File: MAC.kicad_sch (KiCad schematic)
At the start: 5 parts

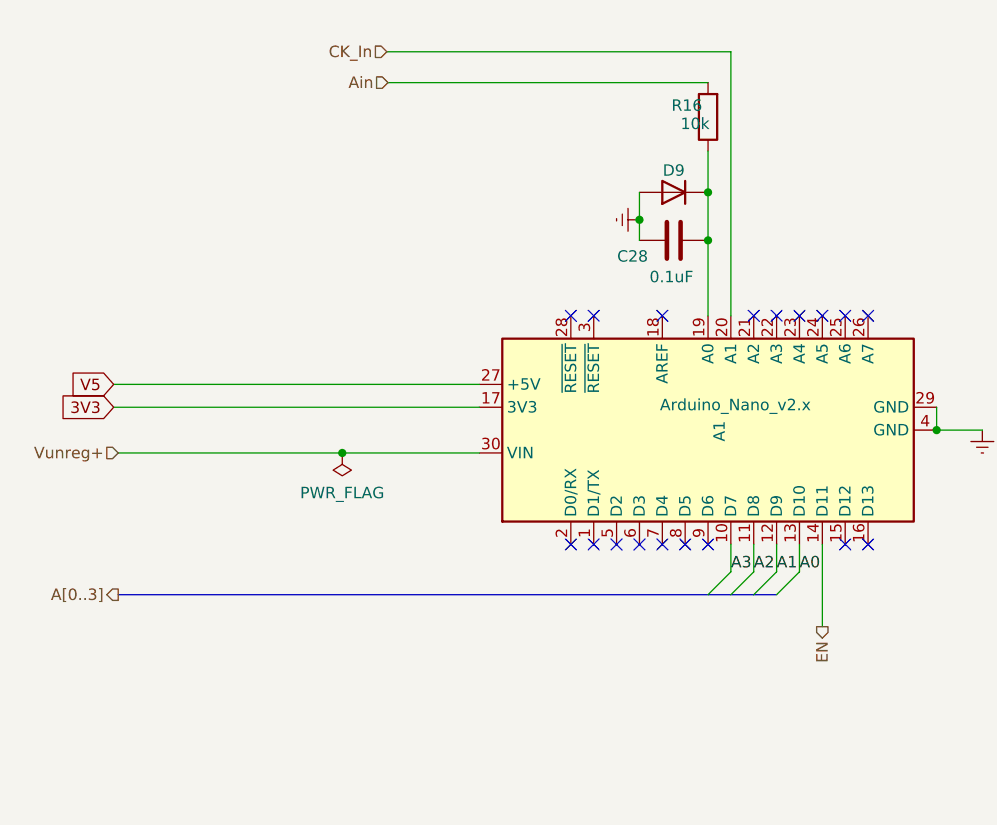
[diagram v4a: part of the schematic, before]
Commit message: Updated improved board for all SMD
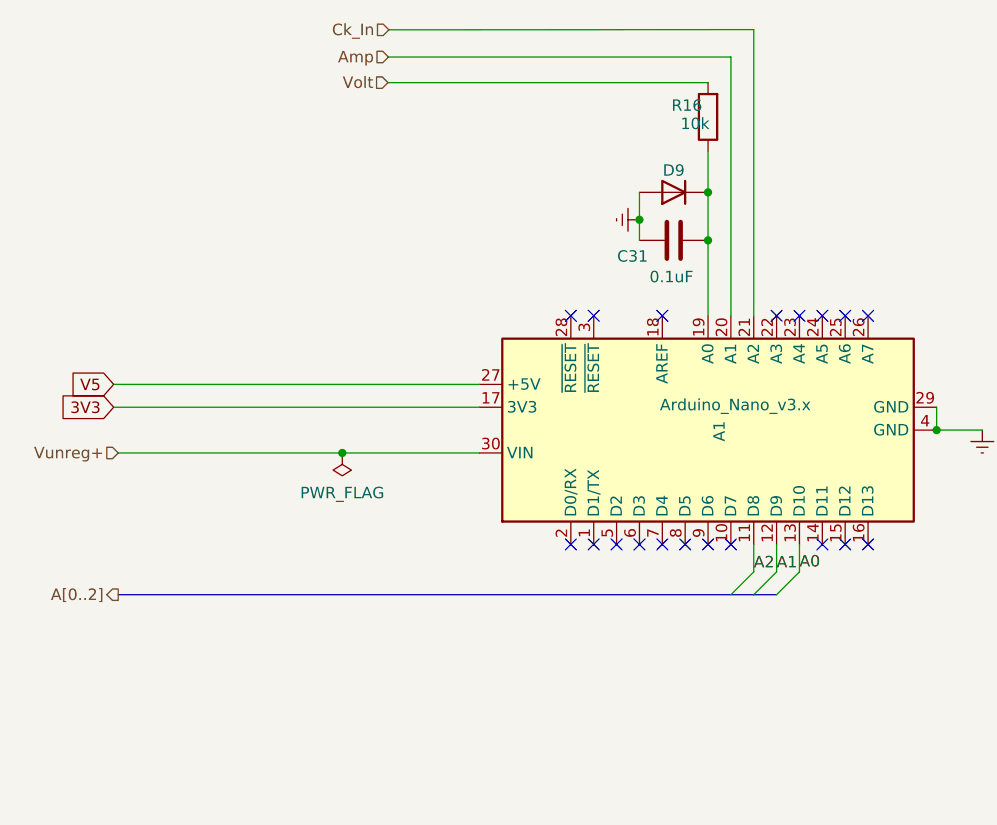
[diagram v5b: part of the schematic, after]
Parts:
- A1: value Arduino_Nano_v2.x -> Arduino_Nano_v3.x; symbol MCU_Module:Arduino_Nano_v2.x -> MCU_Module:Arduino_Nano_v3.x
- renumbered C28 to C31
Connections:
- net Ck_In: now reaches A1.21 (A2)
- net A3: no longer names the net of A1.10 (D7)
- net Ain renamed Volt
- net CK_In renamed Amp
- net EN: no longer names the net of A1.14 (D11)
- no-connect marks 45 -> 46
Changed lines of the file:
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@@
   (junction (at 140.97 74.168) (diameter 0) (color 0 0 0 0)
   )
+  (no_connect (at 143.51 113.284))
   (no_connect (at 212.344 63.754))
   (no_connect (at 209.804 63.754))
@@
   (no_connect (at 148.59 87.884))
   (no_connect (at 153.67 87.884))
-  (no_connect (at 146.05 87.884))
   (no_connect (at 156.21 87.884))
   (no_connect (at 151.13 87.884))
@@
   (no_connect (at 128.27 87.884))
   (no_connect (at 135.89 87.884))
+  (no_connect (at 153.67 113.284))
   (no_connect (at 197.104 81.534))
   (no_connect (at 197.104 122.174))
@@
   (no_connect (at 212.344 139.954))
   (no_connect (at 209.804 139.954))
-  (bus_entry (at 140.97 118.872) (size 2.54 -2.54)
-    (stroke (width 0) (type default) (color 0 0 0 0))
-  )
   (bus_entry (at 143.51 118.872) (size 2.54 -2.54)
     (stroke (width 0) (type default) (color 0 0 0 0))
@@
     (stroke (width 0) (type default) (color 0 0 0 0))
   )
-  (wire (pts (xy 143.51 87.884) (xy 143.51 58.547))
+  (wire (pts (xy 146.05 87.884) (xy 146.05 56.0832))
     (stroke (width 0) (type default) (color 0 0 0 0))
   )
@@
     (stroke (width 0) (type default) (color 0 0 0 0))
   )
-  (bus (pts (xy 140.97 118.872) (xy 143.51 118.872))
-    (stroke (width 0) (type default) (color 0 0 0 0))
-  )
   (wire (pts (xy 74.93 95.504) (xy 115.57 95.504))
     (stroke (width 0) (type default) (color 0 0 0 0))
@@
     (stroke (width 0) (type default) (color 0 0 0 0))
   )
+  (wire (pts (xy 143.51 59.1312) (xy 143.51 87.884))
+    (stroke (width 0) (type default) (color 0 0 0 0))
+  )
   (wire (pts (xy 146.05 113.284) (xy 146.05 116.332))
     (stroke (width 0) (type default) (color 0 0 0 0))
@@
     (stroke (width 0) (type default) (color 0 0 0 0))
   )
-  (bus (pts (xy 75.438 118.872) (xy 140.97 118.872))
+  (bus (pts (xy 75.438 118.872) (xy 143.51 118.872))
     (stroke (width 0) (type default) (color 0 0 0 0))
   )
@@
     (stroke (width 0) (type default) (color 0 0 0 0))
   )
-  (wire (pts (xy 143.51 58.547) (xy 105.283 58.547))
+  (wire (pts (xy 146.05 56.0832) (xy 105.5116 56.1086))
     (stroke (width 0) (type default) (color 0 0 0 0))
   )
@@
     (stroke (width 0) (type default) (color 0 0 0 0))
   )
+  (wire (pts (xy 105.4608 59.1312) (xy 143.51 59.1312))
+    (stroke (width 0) (type default) (color 0 0 0 0))
+  )
   (wire (pts (xy 166.37 100.584) (xy 171.45 100.584))
     (stroke (width 0) (type default) (color 0 0 0 0))
   )
-  (wire (pts (xy 153.67 113.284) (xy 153.67 122.428))
-    (stroke (width 0) (type default) (color 0 0 0 0))
-  )
   (wire (pts (xy 100.33 103.124) (xy 115.57 103.124))
     (stroke (width 0) (type default) (color 0 0 0 0))
   )
-  (wire (pts (xy 143.51 113.284) (xy 143.51 116.332))
-    (stroke (width 0) (type default) (color 0 0 0 0))
-  )
   (wire (pts (xy 148.59 113.284) (xy 148.59 116.332))
     (stroke (width 0) (type default) (color 0 0 0 0))
@@
     (stroke (width 0) (type default) (color 0 0 0 0))
   )
-  (label "A3" (at 143.51 116.332 0)
-    (effects (font (size 1.27 1.27)) (justify left bottom))
-  )
-  (label "A0" (at 151.13 116.332 0)
+  (label "A0" (at 151.13 116.2304 0)
     (effects (font (size 1.27 1.27)) (justify left bottom))
   )
@@
     )
   )
-  (hierarchical_label "EN" (shape output) (at 153.67 122.428 270)
-    (effects (font (size 1.27 1.27)) (justify right))
-  )
-  (hierarchical_label "CK_In" (shape input) (at 105.283 58.547 180)
+  (hierarchical_label "Ck_In" (shape input) (at 105.5116 56.1086 180)
     (effects (font (size 1.27 1.27)) (justify right))
   )
@@
     (effects (font (size 1.27 1.27)) (justify right))
   )
-  (hierarchical_label "A[0..3]" (shape output) (at 75.438 118.872 180)
-    (effects (font (size 1.27 1.27)) (justify right))
-  )
-  (hierarchical_label "Ain" (shape input) (at 105.41 61.976 180)
+  (hierarchical_label "A[0..2]" (shape output) (at 75.438 118.872 180)
+    (effects (font (size 1.27 1.27)) (justify right))
+  )
+  (hierarchical_label "Volt" (shape input) (at 105.41 61.976 180)
+    (effects (font (size 1.27 1.27)) (justify right))
+  )
+  (hierarchical_label "Amp" (shape input) (at 105.4608 59.1312 180)
     (effects (font (size 1.27 1.27)) (justify right))
   )
@@
   (symbol (lib_id "power:PWR_FLAG") (at 100.33 103.124 180) (unit 1)
     (in_bom yes) (on_board yes) (fields_autoplaced)
-    (property "Reference" "#FLG09" (id 0) (at 100.33 105.029 0)
+    (property "Reference" "#FLG03" (id 0) (at 100.33 105.029 0)
       (effects (font (size 1.27 1.27)) hide)
     )
@@
   (symbol (lib_id "power:GNDREF") (at 171.45 100.584 0) (unit 1)
     (in_bom yes) (on_board yes) (fields_autoplaced)
-    (property "Reference" "#PWR025" (id 0) (at 171.45 106.934 0)
+    (property "Reference" "#PWR031" (id 0) (at 171.45 106.934 0)
       (effects (font (size 1.27 1.27)) hide)
     )
@@
   (symbol (lib_id "Device:C") (at 137.16 79.502 90) (unit 1)
     (in_bom yes) (on_board yes)
-    (property "Reference" "C28" (id 0) (at 132.588 81.28 90))
+    (property "Reference" "C31" (id 0) (at 132.588 81.28 90))
     (property "Value" "0.1uF" (id 1) (at 136.906 83.566 90))
     (property "Footprint" "Capacitor_SMD:C_0603_1608Metric" (id 2) (at 140.97 78.5368 0)
@@
     (pin "2")
   )
-  (symbol (lib_id "MCU_Module:Arduino_Nano_v2.x") (at 140.97 100.584 90) (unit 1)
+  (symbol (lib_id "MCU_Module:Arduino_Nano_v3.x") (at 140.97 100.584 90) (unit 1)
     (in_bom yes) (on_board yes)
     (property "Reference" "A1" (id 0) (at 142.24 101.854 0)
       (effects (font (size 1.27 1.27)) (justify left))
     )
-    (property "Value" "Arduino_Nano_v2.x" (id 1) (at 152.4 97.79 90)
+    (property "Value" "Arduino_Nano_v3.x" (id 1) (at 152.4 97.79 90)
       (effects (font (size 1.27 1.27)) (justify left))
     )
@@
       (effects (font (size 1.27 1.27) italic) hide)
     )
-    (property "Datasheet" "https://www.arduino.cc/en/uploads/Main/ArduinoNanoManual23.pdf" (id 3) (at 140.97 100.584 0)
+    (property "Datasheet" "http://www.mouser.com/pdfdocs/Gravitech_Arduino_Nano3_0.pdf" (id 3) (at 140.97 100.584 0)
       (effects (font (size 1.27 1.27)) hide)
     )
@@
   (symbol (lib_id "power:GNDREF") (at 207.264 139.954 0) (unit 1)
     (in_bom yes) (on_board yes) (fields_autoplaced)
-    (property "Reference" "#PWR026" (id 0) (at 207.264 146.304 0)
+    (property "Reference" "#PWR032" (id 0) (at 207.264 146.304 0)
       (effects (font (size 1.27 1.27)) hide)
     )
@@
   (symbol (lib_id "power:GNDREF") (at 133.35 77.216 270) (unit 1)
     (in_bom yes) (on_board yes) (fields_autoplaced)
-    (property "Reference" "#PWR024" (id 0) (at 127 77.216 0)
-      (effects (font (size 1.27 1.27)) hide)
-    )
+    (property "Reference" "#PWR030" (id 0) (at 127 77.216 0)
+      (effects (font (size 1.27 1.27)) hide)
+    )

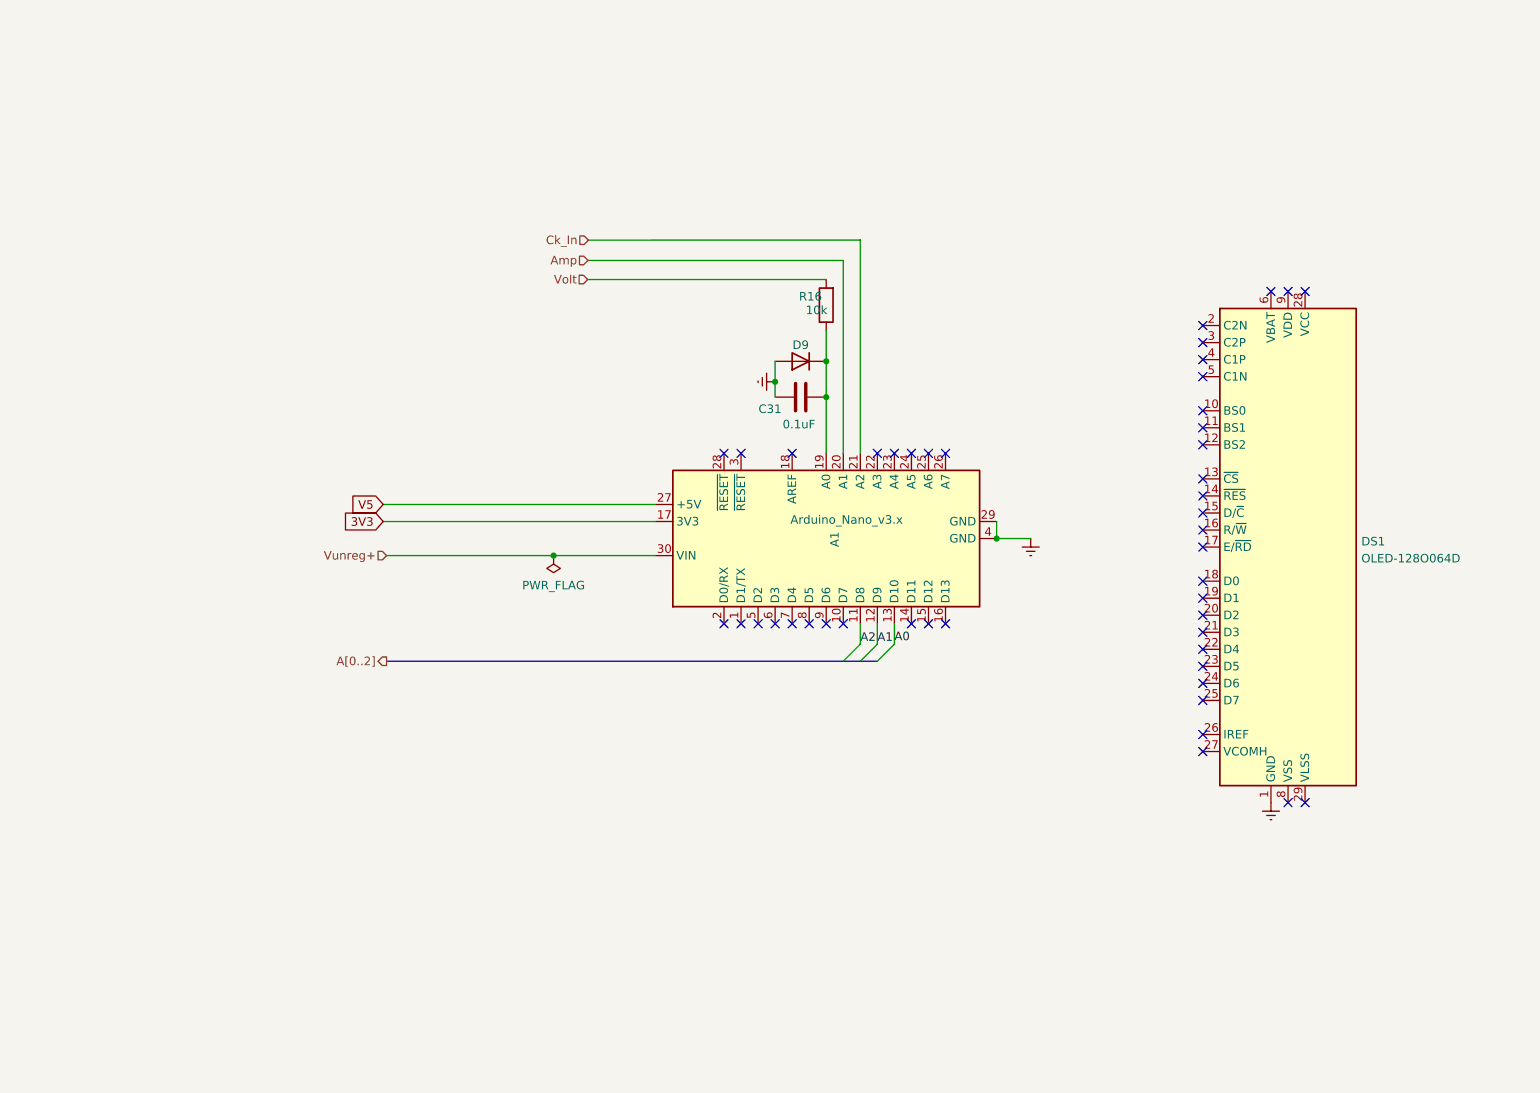
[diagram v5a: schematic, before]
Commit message: further refining board size, adding rotary encoder and OLED display
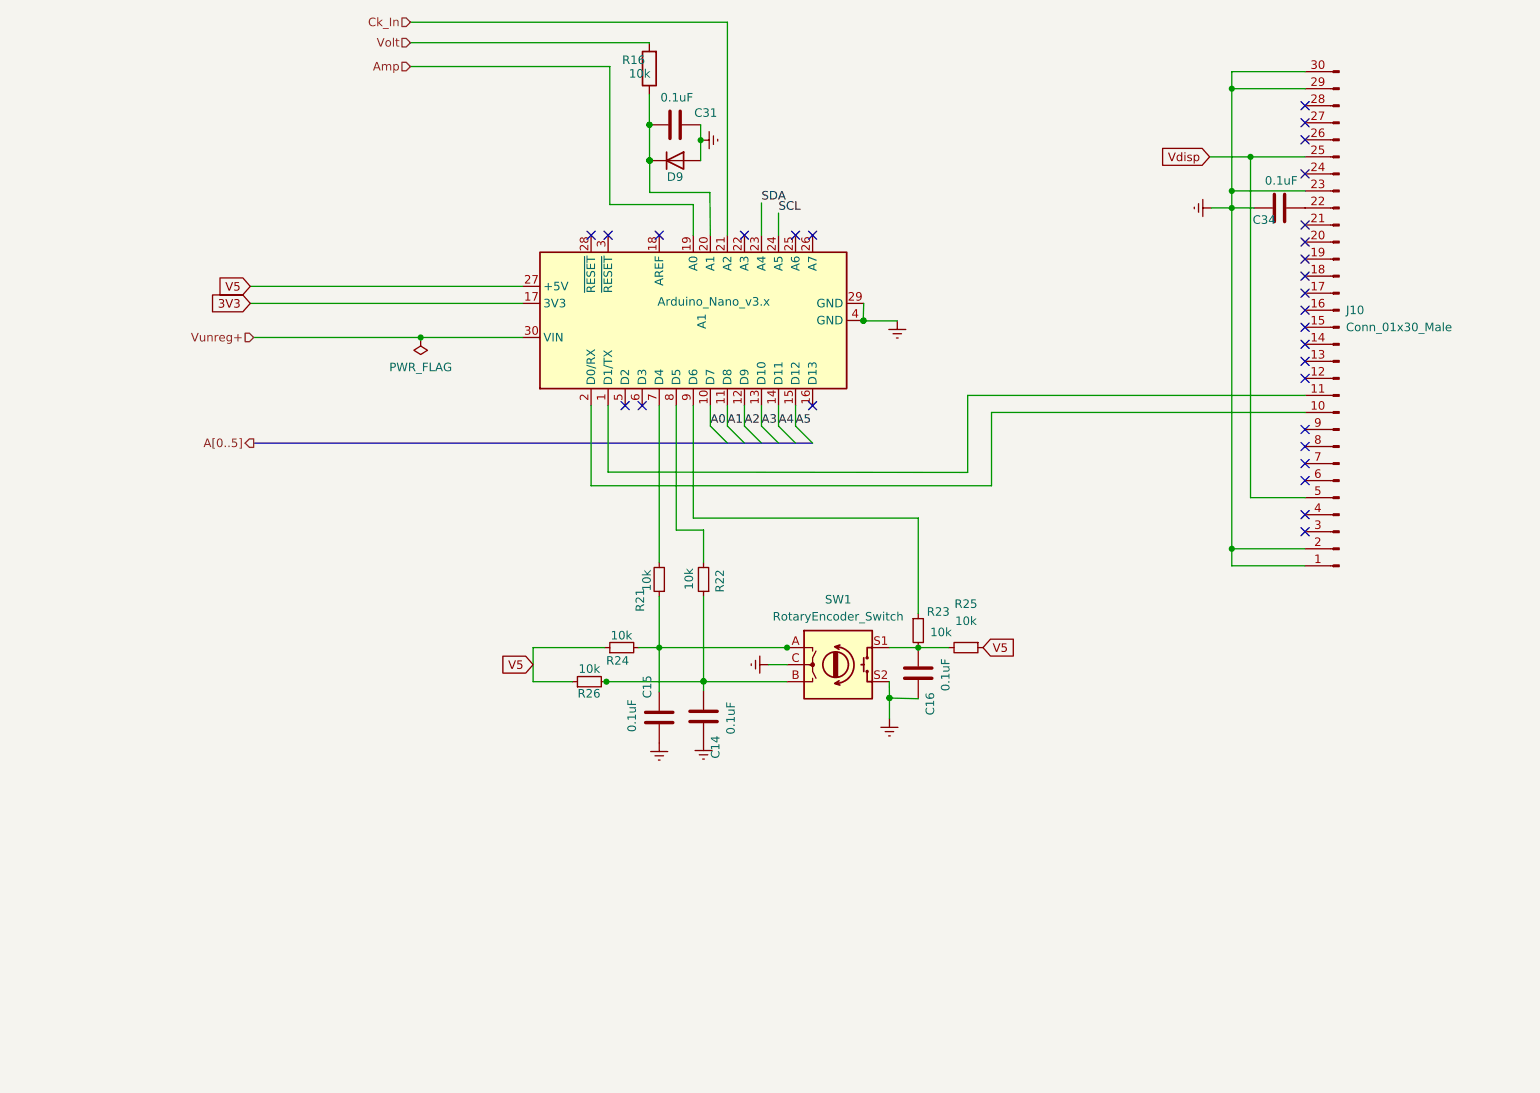
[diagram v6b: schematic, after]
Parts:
- removed DS1: OLED-128O064D, Display:OLED-128O064D, symbol Display_Graphic:OLED-128O064D
- added C14, C15, C16, C34: 0.1uF, Capacitor_SMD:C_0603_1608Metric, symbol Device:C
- added J10: Conn_01x30_Male, WE SMD Side 30 Pin:687130149022, symbol Connector:Conn_01x30_Male
- added R21, R22, R23, R24, R25, R26: 10k, Resistor_SMD:R_0603_1608Metric, symbol Device:R_Small
- added SW1: RotaryEncoder_Switch, Rotary_Encoder:RotaryEncoder_Alps_EC11E_Vertical_H20mm, symbol Device:RotaryEncoder_Switch
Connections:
- net A0: now also A1.10 (D7); no longer A1.13 (D10)
- net A1: now also A1.11 (D8); no longer A1.12 (D9)
- net A2: now also A1.12 (D9); no longer A1.11 (D8)
- net Amp: now also A1.19 (A0); no longer A1.20 (A1)
- net GNDREF: now also C14.1, C15.2, C16.1, C34.2, J10.1 (Pin_1), J10.2 (Pin_2), J10.23 (Pin_23), J10.29 (Pin_29), J10.30 (Pin_30), SW1.C, SW1.S2
- net V5: now also R24.1, R25.1, R26.1
- net at C31.2, D9.2 (K), R16.1: now also A1.20 (A1); no longer A1.19 (A0)
- net at A1.1 (D1/TX): now also J10.11 (Pin_11)
- net A4: now reaches A1.14 (D11)
- net A5: now reaches A1.15 (D12)
- net at A1.2 (D0/RX): now also J10.10 (Pin_10)
- net SDA: now reaches A1.23 (A4)
- net SCL: now reaches A1.24 (A5)
- net at A1.7 (D4): now also R21.2
- net at A1.8 (D5): now also R22.2
- net at A1.9 (D6): now also R23.1
- new net: C16.2, R23.2, R25.2, SW1.S1
- new net: C15.1, R21.1, R24.2, SW1.A
- new net: C14.2, R22.1, R26.2, SW1.B
- new net: C34.1, J10.22 (Pin_22)
- new net A3: A1.13 (D10)
- new net Vdisp: J10.25 (Pin_25), J10.5 (Pin_5)
- no-connect marks 46 -> 29
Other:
- moved on the sheet: A1, C31, D9, R16
